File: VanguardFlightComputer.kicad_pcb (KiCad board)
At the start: 4 copper layers, 56 x 32 mm, 69 parts, among them IC1 ST1L05CPU33R, IC2 ASM330LHHTR, IC3 MAX-M10S-00B, J1 USB_C_Receptacle, J2 MEM2067-02-180-00-A, J3 Conn_Coaxial, J4 Conn_Coaxial, J5 Conn_01x04_Pin, J6 Conn_01x02_Pin, J7 Conn_01x04_Pin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

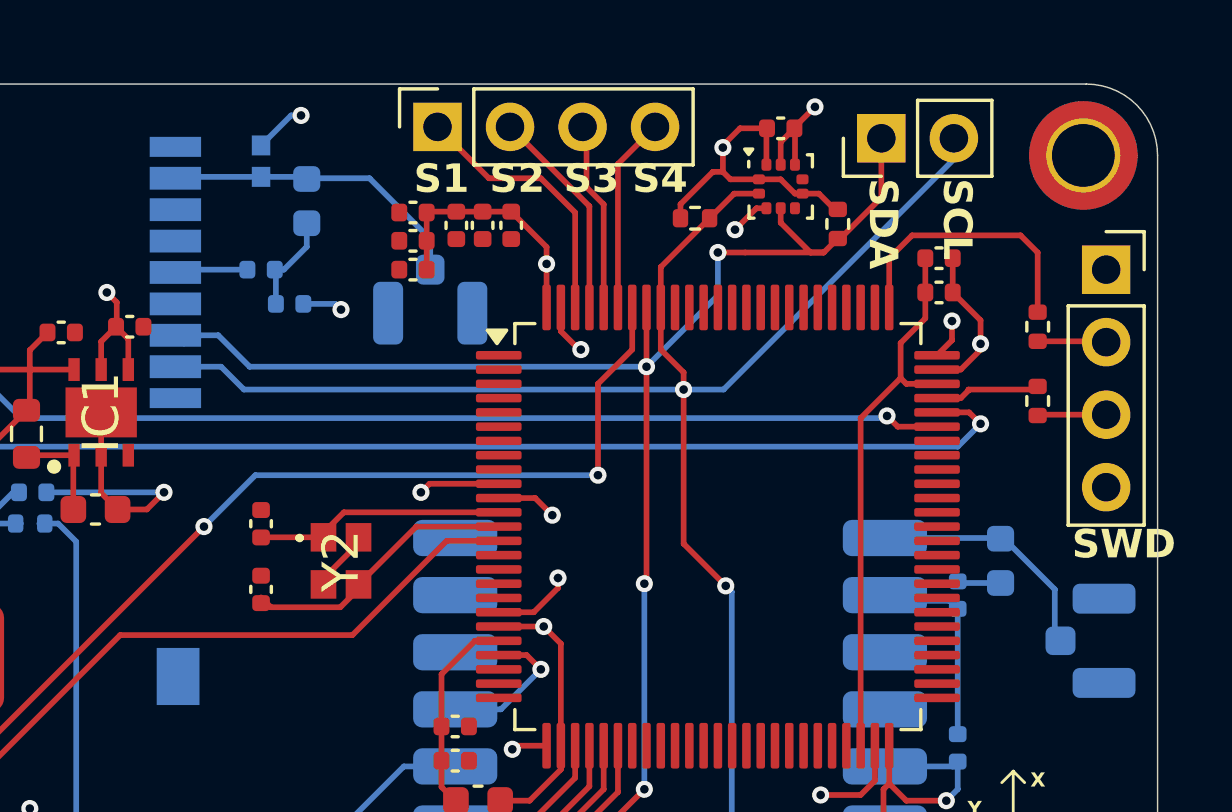
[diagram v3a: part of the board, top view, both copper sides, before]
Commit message: Impedence match trace
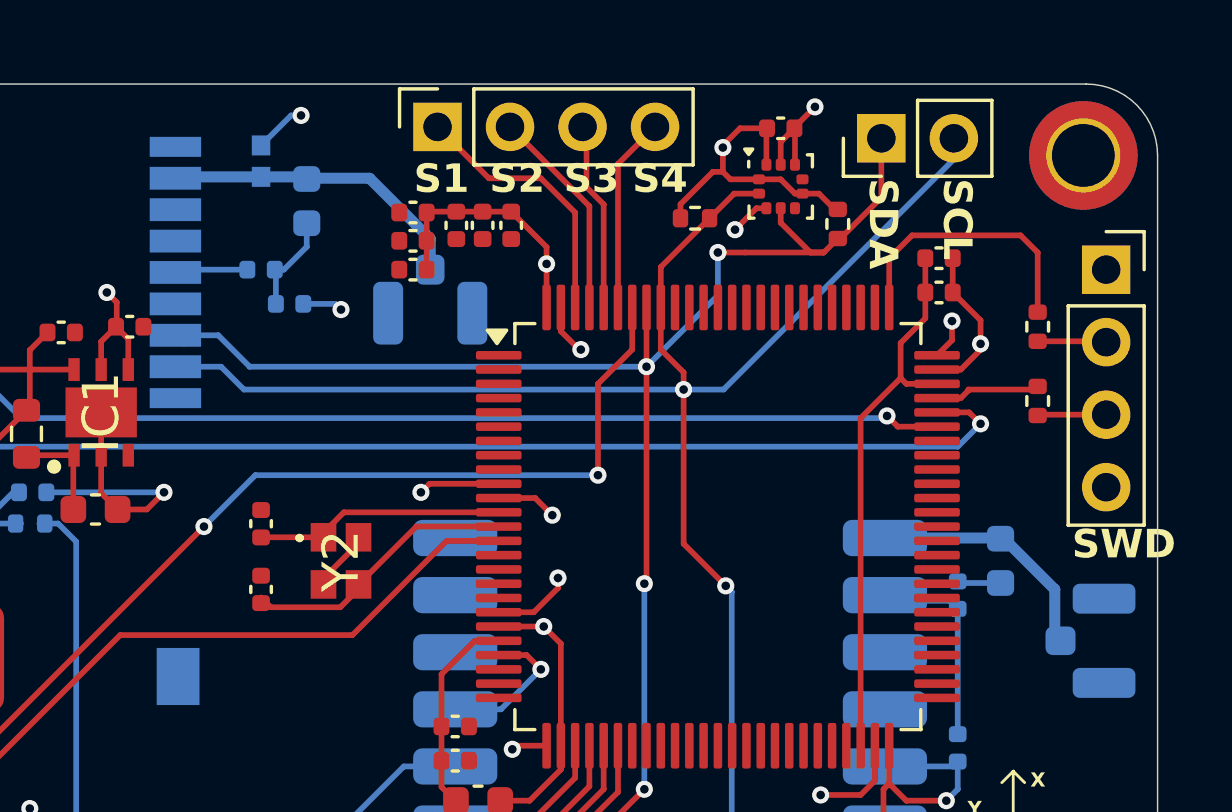
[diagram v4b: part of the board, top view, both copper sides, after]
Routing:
- added copper zone on In1.Cu, net +3.3V
- added copper zone on In2.Cu, net GND
- removed copper zone on In2.Cu, net +3.3V
- removed copper zone on In1.Cu, net GND
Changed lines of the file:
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@@
 	(layers
 		(0 "F.Cu" signal)
-		(1 "In1.Cu" signal "In1.GND")
-		(2 "In2.Cu" signal "In2.PWR")
+		(1 "In1.Cu" signal "In1.PWR")
+		(2 "In2.Cu" signal "In2.GND")
 		(31 "B.Cu" signal)
 		(32 "B.Adhes" user "B.Adhesive")
@@
 		(sheetname "IO")
 		(sheetfile "io.kicad_sch")
-		(zone_connect 0)
 		(attr smd)
 		(fp_line
@@
 			(at 0 0 90)
 			(layer "B.SilkS")
+			(hide yes)
 			(effects
 				(font
@@
 			(at 0 0 0)
 			(layer "B.SilkS")
+			(hide yes)
 			(effects
 				(font
@@
 			(at 0 4.825 0)
 			(layer "B.SilkS")
+			(hide yes)
 			(effects
 				(font
@@
 		(remove_unused_layers yes)
 		(keep_end_layers yes)
-		(zone_layer_connections "In1.Cu")
+		(zone_layer_connections "In2.Cu")
 		(net 2)
 	)
@@
 		(remove_unused_layers yes)
 		(keep_end_layers yes)
-		(zone_layer_connections "In1.Cu")
+		(zone_layer_connections "In2.Cu")
 		(net 2)
 	)
@@
 		(remove_unused_layers yes)
 		(keep_end_layers yes)
-		(zone_layer_connections "In1.Cu")
+		(zone_layer_connections "In2.Cu")
 		(net 2)
 	)
@@
 		(remove_unused_layers yes)
 		(keep_end_layers yes)
-		(zone_layer_connections "In1.Cu")
+		(zone_layer_connections "In2.Cu")
 		(net 2)
 	)
@@
 		(remove_unused_layers yes)
 		(keep_end_layers yes)
-		(zone_layer_connections "In1.Cu")
+		(zone_layer_connections "In2.Cu")
 		(net 2)
 	)
@@
 		(keep_end_layers yes)
 		(free yes)
-		(zone_layer_connections "In1.Cu")
+		(zone_layer_connections "In2.Cu")
 		(net 2)
 	)
@@
 		(remove_unused_layers yes)
 		(keep_end_layers yes)
-		(zone_layer_connections "In1.Cu")
+		(zone_layer_connections "In2.Cu")
 		(net 2)
 	)
@@
 		(remove_unused_layers yes)
 		(keep_end_layers yes)
-		(zone_layer_connections "In1.Cu")
+		(zone_layer_connections "In2.Cu")
 		(net 2)
 	)
@@
 		(remove_unused_layers yes)
 		(keep_end_layers yes)
-		(zone_layer_connections "In1.Cu")
+		(zone_layer_connections "In2.Cu")
 		(net 2)
 	)
@@
 		(remove_unused_layers yes)
 		(keep_end_layers yes)
-		(zone_layer_connections "In1.Cu")
+		(zone_layer_connections "In2.Cu")
 		(net 2)
 	)
@@
 		(remove_unused_layers yes)
 		(keep_end_layers yes)
-		(zone_layer_connections "In1.Cu")
+		(zone_layer_connections "In2.Cu")
 		(net 2)
 	)
@@
 		(remove_unused_layers yes)
 		(keep_end_layers yes)
-		(zone_layer_connections "In1.Cu")
+		(zone_layer_connections "In2.Cu")
 		(net 2)
 	)
@@
 		(remove_unused_layers yes)
 		(keep_end_layers yes)
-		(zone_layer_connections "In1.Cu")
+		(zone_layer_connections "In2.Cu")
 		(net 2)
 	)
@@
 		(remove_unused_layers yes)
 		(keep_end_layers yes)
-		(zone_layer_connections "In1.Cu")
+		(zone_layer_connections "In2.Cu")
 		(net 2)
 	)
@@
 		(remove_unused_layers yes)
 		(keep_end_layers yes)
-		(zone_layer_connections "In1.Cu")
+		(zone_layer_connections "In2.Cu")
 		(net 2)
 	)
@@
 		(remove_unused_layers yes)
 		(keep_end_layers yes)
-		(zone_layer_connections "In2.Cu")
+		(zone_layer_connections "In1.Cu")
 		(net 3)
 	)
@@
 		(remove_unused_layers yes)
 		(keep_end_layers yes)
-		(zone_layer_connections "In2.Cu")
+		(zone_layer_connections "In1.Cu")
 		(net 3)
 	)
@@
 		(remove_unused_layers yes)
 		(keep_end_layers yes)
-		(zone_layer_connections "In2.Cu")
+		(zone_layer_connections "In1.Cu")
 		(net 3)
 	)
@@
 		(remove_unused_layers yes)
 		(keep_end_layers yes)
-		(zone_layer_connections "In2.Cu")
+		(zone_layer_connections "In1.Cu")
 		(net 3)
 	)
@@
 		(remove_unused_layers yes)
 		(keep_end_layers yes)
-		(zone_layer_connections "In2.Cu")
+		(zone_layer_connections "In1.Cu")
 		(net 3)
 	)
@@
 		(remove_unused_layers yes)
 		(keep_end_layers yes)
-		(zone_layer_connections "In2.Cu")
+		(zone_layer_connections "In1.Cu")
 		(net 3)
 	)
@@
 		(remove_unused_layers yes)
 		(keep_end_layers yes)
-		(zone_layer_connections "In2.Cu")
+		(zone_layer_connections "In1.Cu")
 		(net 3)
 	)
@@
 		(remove_unused_layers yes)
 		(keep_end_layers yes)
-		(zone_layer_connections "In2.Cu")
+		(zone_layer_connections "In1.Cu")
 		(net 3)
 	)
@@
 		(remove_unused_layers yes)
 		(keep_end_layers yes)
-		(zone_layer_connections "In2.Cu")
+		(zone_layer_connections "In1.Cu")
 		(net 3)
 	)
@@
 		(remove_unused_layers yes)
 		(keep_end_layers yes)
-		(zone_layer_connections "In2.Cu")
+		(zone_layer_connections "In1.Cu")
 		(net 3)
 	)
@@
 		(start 120.525 82)
 		(end 120.525 80.925)
-		(width 0.2)
+		(width 0.38735)
 		(layer "B.Cu")
 		(net 122)
@@
 		(start 120.525 80.925)
 		(end 118.4 78.8)
-		(width 0.2)
+		(width 0.38735)
 		(layer "B.Cu")
 		(net 122)
@@
 		(start 114.6 78.75)
 		(end 116.125 78.75)
-		(width 0.2)
+		(width 0.38735)
 		(layer "B.Cu")
 		(net 122)
@@
 		(start 114.6 78.75)
 		(end 111.65 78.75)
-		(width 0.2)
+		(width 0.38735)
 		(layer "B.Cu")
 		(net 122)
@@
 		(start 118.4 78.8)
 		(end 116.225 78.8)
-		(width 0.2)
+		(width 0.38735)
 		(layer "B.Cu")
 		(net 122)
@@
 		(start 142.4 93.2)
 		(end 142.4 94.8)
-		(width 0.2)
+		(width 0.38735)
 		(layer "B.Cu")
 		(net 143)
@@
 		(start 140.625 91.425)
 		(end 142.4 93.2)
-		(width 0.2)
+		(width 0.38735)
 		(layer "B.Cu")
 		(net 143)
@@
 		(start 136.45 91.4)
 		(end 140.475 91.4)
-		(width 0.2)
+		(width 0.38735)
 		(layer "B.Cu")
 		(net 143)
@@
 	)
 	(zone
-		(net 2)
-		(net_name "GND")
+		(net 3)
+		(net_name "+3.3V")
 		(layer "In1.Cu")
 		(hatch edge 0.5)
@@
 	)
 	(zone
-		(net 3)
-		(net_name "+3.3V")
+		(net 2)
+		(net_name "GND")
 		(layer "In2.Cu")
 		(hatch edge 0.5)

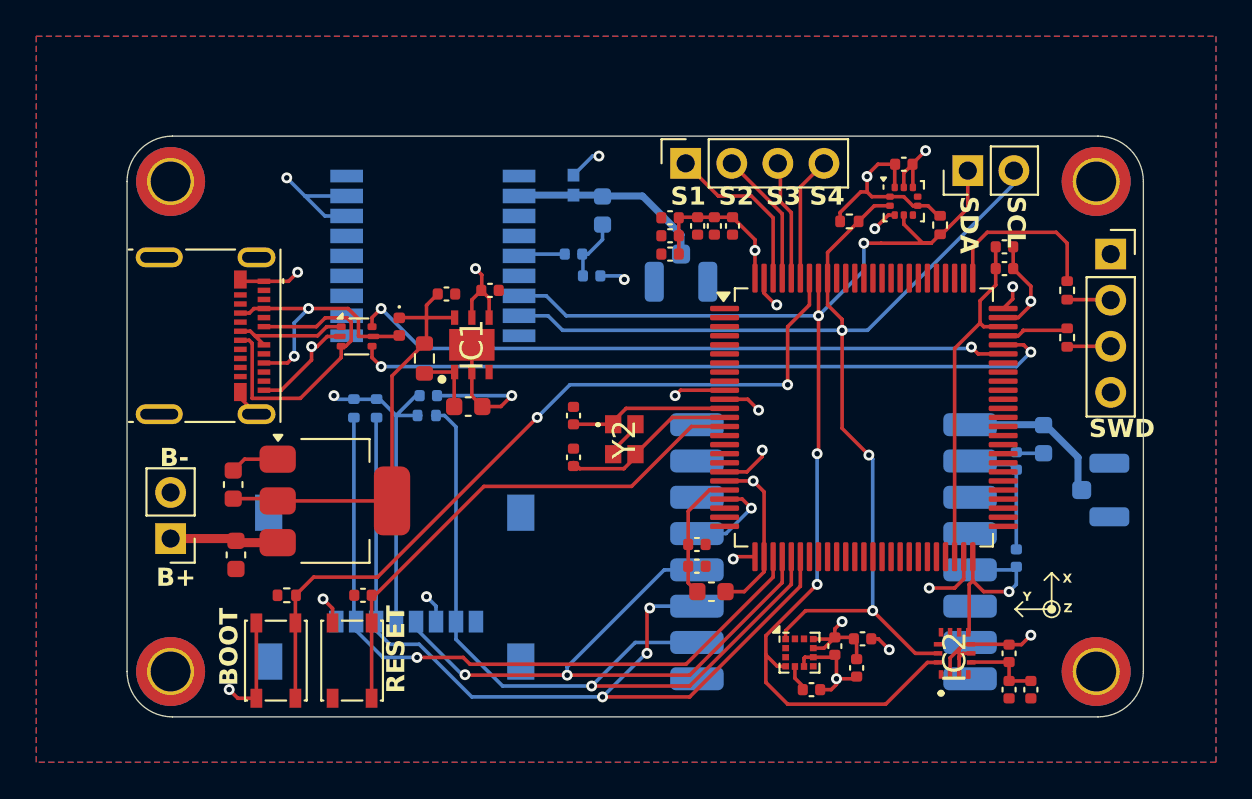
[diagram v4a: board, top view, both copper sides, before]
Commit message: Added STM32_MX Project, LED, Fixed DRC Violations
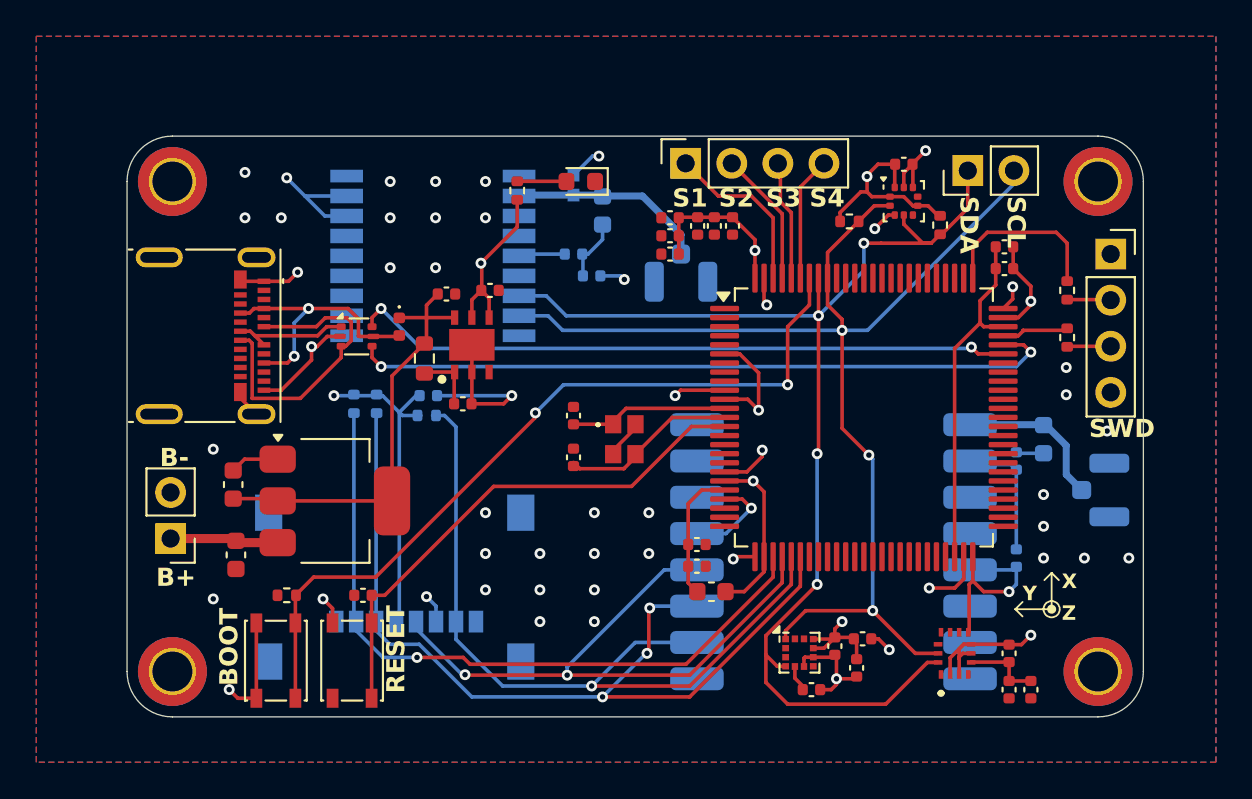
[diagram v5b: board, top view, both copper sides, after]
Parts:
- removed U1: STM32H743VGTx, Package_QFP:LQFP-100_14x14mm_P0.5mm
- added D3: LED, LED_SMD:LED_0603_1608Metric, F.Cu at (115.0, 78.0)
- added R11: 220, Resistor_SMD:R_0402_1005Metric, F.Cu at (111.5, 78.5)
- added U6: STM32H743VITx, Package_QFP:LQFP-100_14x14mm_P0.5mm, F.Cu at (130.6, 91.0)
- C13: footprint Capacitor_SMD:C_0603_1608Metric -> Capacitor_SMD:C_0402_1005Metric
- moved C13 0.34 mm to (108.5, 90.2)
- moved R4 0.25 mm to (102.5, 90.2)
- moved R5 0.25 mm to (103.8, 90.2)
- moved H1 0.10 mm to (92.5, 78.0)
- moved H5 0.10 mm to (143.5, 78.0)
- moved H6 0.10 mm to (92.5, 105.0)
- moved H7 0.10 mm to (143.5, 105.0)
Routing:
- net +3.3V: track 85.2 -> 94.1 mm
- net Net-(D3-A): track 0.00 -> 2.72 mm
- net SPI1_MOSI: track 49.5 -> 50.0 mm
- net GND: track 78.0 -> 77.9 mm, vias 18 -> 51
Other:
- board text added: "0"
- board text added: "0 mm"
- board text added: "0.0000 mm / 0.0000 mm"
- board text added: "0.0091"
- board text added: "0.0152 mm"
- board text added: "0.0175 mm"
- board text added: "0.0432 mm"
- board text added: "0.1999 mm"
- board text added: "0.3000 mm"
- board text added: "0.9906 mm"
- board text added: "1"
- board text added: "1.5422 mm"
- board text added: "3.3"
- board text added: "3.69"
- board text added: "4"
- board text added: "56.0000 mm x 32.0000 mm"
- board text added: "B.Cu"
- board text added: "B.Mask"
- board text added: "B.Paste"
- board text added: "B.Silkscreen"
- board text added: "BOARD CHARACTERISTICS"
- board text added: "Board Thickness:"
- board text added: "Board overall dimensions:"
- board text added: "Bottom Silk Screen"
- board text added: "Bottom Solder Mask"
- board text added: "Bottom Solder Paste"
- board text added: "Castellated pads:"
- board text added: "Color"
- board text added: "Copper Finish:"
- board text added: "Copper Layer Count:"
- board text added: "Dielectric"
- board text added: "Edge card connectors:"
- board text added: "Epsilon R"
- board text added: "F.Cu"
- board text added: "F.Mask"
- board text added: "F.Paste"
- board text added: "F.Silkscreen"
- board text added: "FR4 natural"
- board text added: "FR408-HR"
- board text added: "Impedance Control:"
- board text added: "In1.PWR"
- board text added: "In2.GND"
- board text added: "Layer Name"
- board text added: "Loss Tangent"
- board text added: "Material"
- board text added: "Min hole diameter:"
- board text added: "Min track/spacing:"
- board text added: "No"
- board text added: "None"
- board text added: "Not specified"
- board text added: "Plated Board Edge:"
- board text added: "Purple"
- board text added: "Thickness (mm)"
- board text added: "Top Silk Screen"
- board text added: "Top Solder Mask"
- board text added: "Top Solder Paste"
- board text added: "Type"
- board text added: "White"
- board text added: "Yes"
- board text added: "copper"
- board text added: "core"
- board text added: "prepreg"

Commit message: Aligned IMU axes and fixed JLC match trace
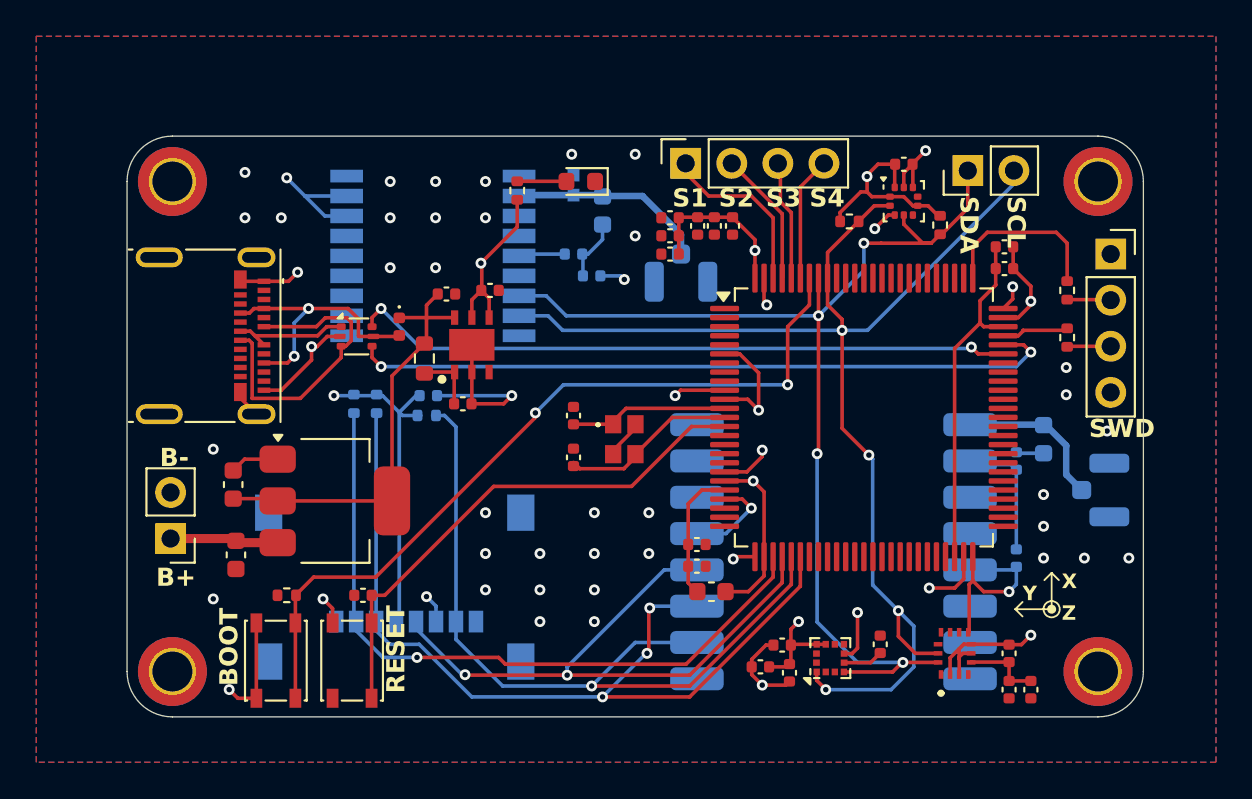
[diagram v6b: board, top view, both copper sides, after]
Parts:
- moved C25 5.30 mm to (124.9, 104.7), turned to 180 degrees
- moved C23 4.54 mm to (131.5, 103.5), turned to 90 degrees
- moved C24 4.44 mm to (126.5, 105.1), turned to -90 degrees
- moved C26 2.90 mm to (126.1, 103.5), turned to 180 degrees
- moved U4 1.73 mm to (128.8, 104.3), turned to 90 degrees
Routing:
- net I2C1_SDA: track 69.3 -> 63.5 mm
- net I2C1_SCL: track 67.2 -> 71.5 mm, vias 3 -> 4
- net GND: track 77.9 -> 76.8 mm, vias 51 -> 53
- net Net-(U4-C1): track 1.45 -> 2.21 mm
